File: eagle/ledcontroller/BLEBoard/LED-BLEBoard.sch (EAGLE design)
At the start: 18 parts, among them U1 FTSH-105-01-F-DV-ND, U2 RFD22301, U3 TPS61232, U4 V_REG_MIC2920, U5 7AAF-3

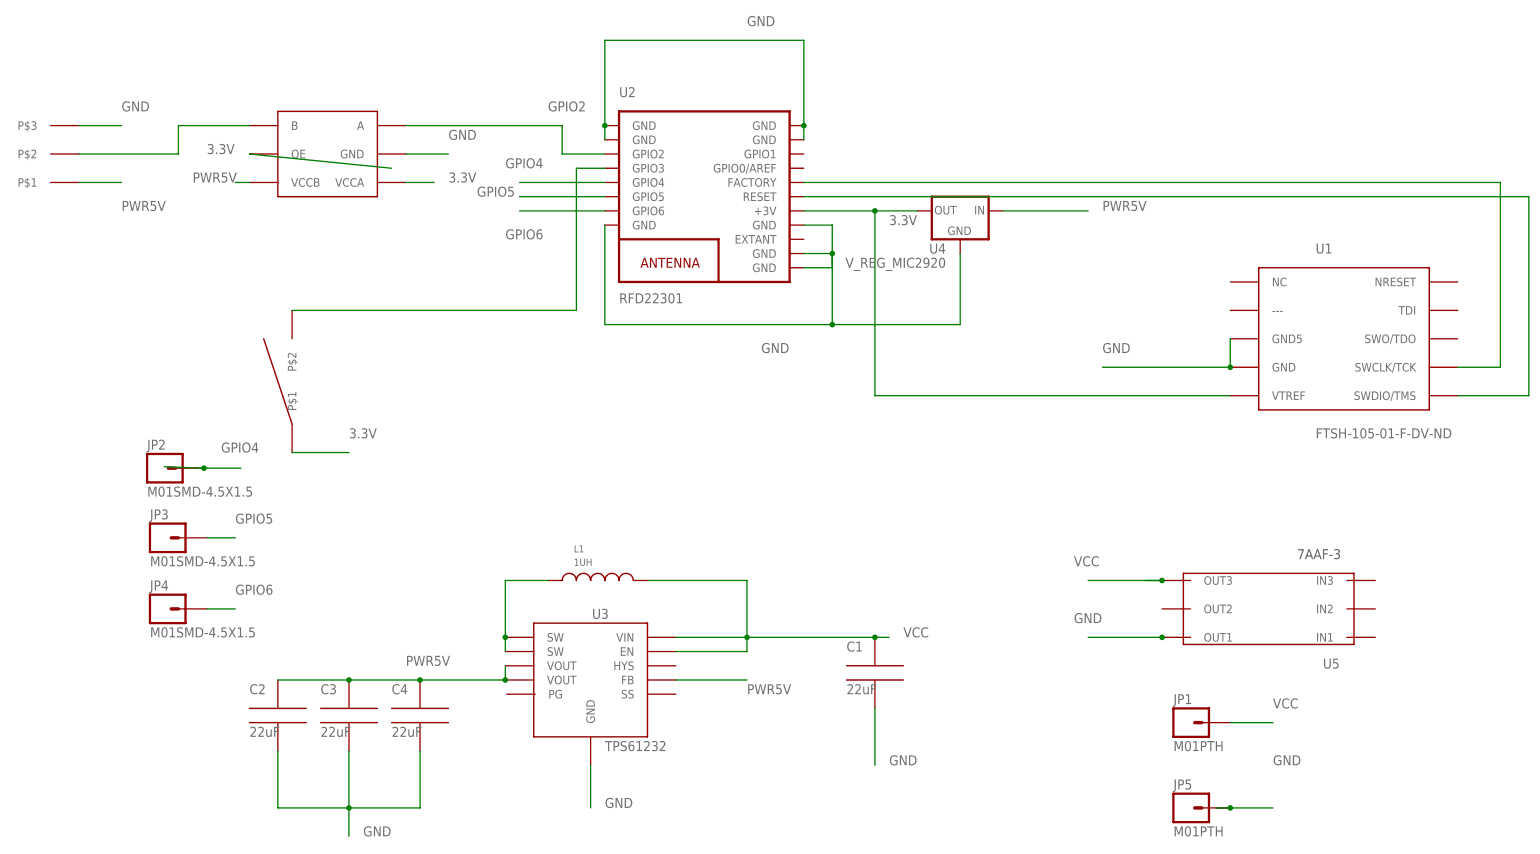
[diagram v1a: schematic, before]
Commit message: V0.8 added switch and re-layout
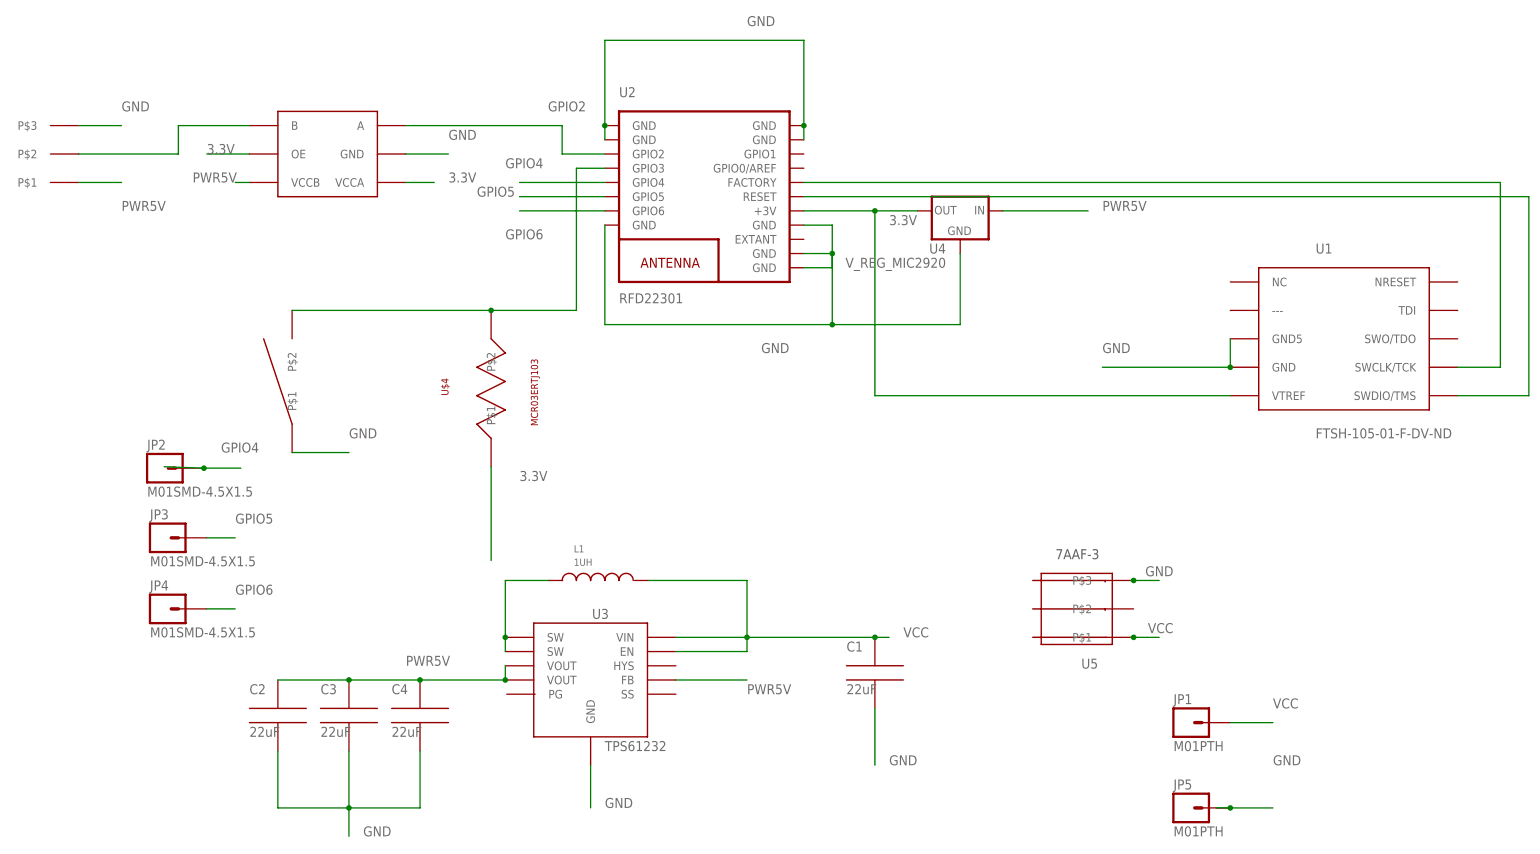
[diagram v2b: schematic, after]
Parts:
- added U$4: MCR03ERTJ103, bret:MCR03ERTJ103
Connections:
- net 3.3V: now also U$4.P$1; no longer U$3.P$1
- net GND: now also U$3.P$1, U5.P$3; no longer U5.OUT1
- net N$2: now also U$4.P$2
- net VCC: now also U5.P$1; no longer U5.OUT3
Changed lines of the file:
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@@
 <part name="JP1" library="SparkFun-Connectors" deviceset="M01" device="PTH"/>
 <part name="JP5" library="SparkFun-Connectors" deviceset="M01" device="PTH"/>
+<part name="U$4" library="bret" deviceset="MCR03ERTJ103" device=""/>
 </parts>
 <sheets>
@@
 <instance part="U1" gate="G$1" x="185.42" y="116.84"/>
 <instance part="U2" gate="G$1" x="48.26" y="139.7"/>
-<instance part="U5" gate="G$1" x="154.178" y="72.39" rot="R90"/>
+<instance part="U5" gate="G$1" x="110.998" y="72.39" rot="R90"/>
 <instance part="U$2" gate="G$1" x="-10.16" y="139.7" rot="R90"/>
 <instance part="U$1" gate="G$1" x="-63.5" y="142.24" rot="R90"/>
@@
 <instance part="JP1" gate="G$1" x="134.62" y="45.72"/>
 <instance part="JP5" gate="G$1" x="134.62" y="30.48"/>
+<instance part="U$4" gate="G$1" x="10.16" y="93.98" rot="R90"/>
 </instances>
 <busses>
@@
 </segment>
 <segment>
-<wire x1="127" y1="71.12" x2="130.048" y2="71.12" width="0.1524" layer="91"/>
-<label x="114.3" y="73.66" size="1.778" layer="95"/>
-<pinref part="U5" gate="G$1" pin="OUT3"/>
-<wire x1="130.048" y1="71.12" x2="116.84" y2="71.12" width="0.1524" layer="91"/>
-<junction x="130.048" y="71.12"/>
-</segment>
-<segment>
 <wire x1="142.24" y1="45.72" x2="149.86" y2="45.72" width="0.1524" layer="91"/>
 <label x="149.86" y="48.26" size="1.778" layer="95"/>
 <pinref part="JP1" gate="G$1" pin="1"/>
+</segment>
+<segment>
+<wire x1="129.54" y1="60.96" x2="124.968" y2="60.96" width="0.1524" layer="91"/>
+<pinref part="U5" gate="G$1" pin="P$1"/>
+<wire x1="124.968" y1="60.96" x2="124.46" y2="60.96" width="0.1524" layer="91"/>
+<junction x="124.968" y="60.96"/>
+<label x="132.08" y="63.5" size="1.778" layer="95" rot="R180"/>
 </segment>
 </net>
@@
 </segment>
 <segment>
-<wire x1="129.54" y1="60.96" x2="130.048" y2="60.96" width="0.1524" layer="91"/>
-<label x="114.3" y="63.5" size="1.778" layer="95"/>
-<pinref part="U5" gate="G$1" pin="OUT1"/>
-<wire x1="130.048" y1="60.96" x2="116.84" y2="60.96" width="0.1524" layer="91"/>
-<junction x="130.048" y="60.96"/>
-</segment>
-<segment>
 <wire x1="139.7" y1="30.48" x2="142.24" y2="30.48" width="0.1524" layer="91"/>
 <label x="149.86" y="38.1" size="1.778" layer="95"/>
@@
 <wire x1="-63.5" y1="152.4" x2="-55.88" y2="152.4" width="0.1524" layer="91"/>
 <label x="-55.88" y="154.94" size="1.778" layer="95"/>
+</segment>
+<segment>
+<pinref part="U$3" gate="G$1" pin="P$1"/>
+<wire x1="-25.4" y1="93.98" x2="-15.24" y2="93.98" width="0.1524" layer="91"/>
+<label x="-15.24" y="96.52" size="1.778" layer="95"/>
+</segment>
+<segment>
+<wire x1="129.54" y1="71.12" x2="124.968" y2="71.12" width="0.1524" layer="91"/>
+<pinref part="U5" gate="G$1" pin="P$3"/>
+<wire x1="124.968" y1="71.12" x2="124.46" y2="71.12" width="0.1524" layer="91"/>
+<junction x="124.968" y="71.12"/>
+<label x="132.08" y="73.66" size="1.778" layer="95" rot="R180"/>
 </segment>
 </net>
@@
 <segment>
 <pinref part="U$2" gate="G$1" pin="OE"/>
-<wire x1="-33.02" y1="147.32" x2="-7.62" y2="144.78" width="0.1524" layer="91"/>
+<wire x1="-33.02" y1="147.32" x2="-40.64" y2="147.32" width="0.1524" layer="91"/>
 <label x="-40.64" y="147.32" size="1.778" layer="95"/>
 </segment>
@@
 </segment>
 <segment>
-<pinref part="U$3" gate="G$1" pin="P$1"/>
-<wire x1="-25.4" y1="93.98" x2="-15.24" y2="93.98" width="0.1524" layer="91"/>
-<label x="-15.24" y="96.52" size="1.778" layer="95"/>
+<wire x1="10.16" y1="74.676" x2="10.16" y2="91.44" width="0.1524" layer="91"/>
+<label x="15.24" y="88.9" size="1.778" layer="95"/>
+<pinref part="U$4" gate="G$1" pin="P$1"/>
 </segment>
 </net>
@@
 <wire x1="25.4" y1="144.78" x2="25.4" y2="119.38" width="0.1524" layer="91"/>
 <pinref part="U$3" gate="G$1" pin="P$2"/>
-<wire x1="25.4" y1="119.38" x2="-25.4" y2="119.38" width="0.1524" layer="91"/>
+<wire x1="25.4" y1="119.38" x2="10.16" y2="119.38" width="0.1524" layer="91"/>
 <pinref part="U2" gate="G$1" pin="GPIO3"/>
+<wire x1="10.16" y1="119.38" x2="-25.4" y2="119.38" width="0.1524" layer="91"/>
 <wire x1="25.4" y1="144.78" x2="30.48" y2="144.78" width="0.1524" layer="91"/>
-</segment>
-</net>
+<pinref part="U$4" gate="G$1" pin="P$2"/>
+<junction x="10.16" y="119.38"/>
+</segment>
+</net>

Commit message: beginning
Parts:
- removed U4: V_REG_MIC2920, SparkFun-PowerIC:V_REG_MIC2920
- U5: value 7AAF-3 -> (none); device bret:7AAF-3 -> bret:TCR2EF33LM
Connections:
- net 3.3V: now also U5.VOUT; no longer U4.OUT
- net GND: now also U5.GND; no longer U4.GND, U5.P$3
- net PWR5V: now also U5.CTRL, U5.VIN; no longer U4.IN
- net VCC: no longer U5.P$1
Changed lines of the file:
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@@
 <setting verticaltext="up"/>
 </settings>
-<grid distance="0.1" unitdist="inch" unit="mm" style="lines" multiple="1" display="no" altdistance="0.01" altunitdist="inch" altunit="inch"/>
+<grid distance="0.1" unitdist="inch" unit="inch" style="lines" multiple="1" display="no" altdistance="0.01" altunitdist="inch" altunit="inch"/>
 <layers>
 <layer number="1" name="Top" color="4" fill="1" visible="no" active="no"/>
@@
 <part name="C1" library="bret" deviceset="C1.6X0.8MM" device="" value="22uF"/>
 <part name="U3" library="bret" deviceset="TPS61232" device="VSON" value="TPS61232"/>
-<part name="U4" library="SparkFun-PowerIC" deviceset="V_REG_MIC2920" device=""/>
 <part name="U1" library="bret" deviceset="FTSH-105-01-XXX-DV-K" device="" value="FTSH-105-01-F-DV-ND"/>
 <part name="U2" library="RF_Digital_RFD22301_Eagle_Schematic_PCB_Library" deviceset="RFD22301" device=""/>
-<part name="U5" library="bret" deviceset="7AAF-3" device="" value="7AAF-3"/>
 <part name="U$2" library="bret" deviceset="TXS0101" device="TXS0101DBVR" value="TXS0101TXS0101DBVR"/>
 <part name="U$1" library="bret" deviceset="MM800" device=""/>
@@
 <part name="JP5" library="SparkFun-Connectors" deviceset="M01" device="PTH"/>
 <part name="U$4" library="bret" deviceset="MCR03ERTJ103" device=""/>
+<part name="U5" library="bret" deviceset="TCR2EF33LM" device=""/>
 </parts>
 <sheets>
@@
 <instance part="C1" gate="G$1" x="81.28" y="45.72"/>
 <instance part="U3" gate="U1" x="27.94" y="53.34"/>
-<instance part="U4" gate="G$1" x="93.98" y="137.16" rot="MR0"/>
 <instance part="U1" gate="G$1" x="185.42" y="116.84"/>
 <instance part="U2" gate="G$1" x="48.26" y="139.7"/>
-<instance part="U5" gate="G$1" x="110.998" y="72.39" rot="R90"/>
 <instance part="U$2" gate="G$1" x="-10.16" y="139.7" rot="R90"/>
 <instance part="U$1" gate="G$1" x="-63.5" y="142.24" rot="R90"/>
@@
 <instance part="JP5" gate="G$1" x="134.62" y="30.48"/>
 <instance part="U$4" gate="G$1" x="10.16" y="93.98" rot="R90"/>
+<instance part="U5" gate="G$1" x="96.52" y="132.08"/>
 </instances>
 <busses>
@@
 <pinref part="JP1" gate="G$1" pin="1"/>
 </segment>
-<segment>
-<wire x1="129.54" y1="60.96" x2="124.968" y2="60.96" width="0.1524" layer="91"/>
-<pinref part="U5" gate="G$1" pin="P$1"/>
-<wire x1="124.968" y1="60.96" x2="124.46" y2="60.96" width="0.1524" layer="91"/>
-<junction x="124.968" y="60.96"/>
-<label x="132.08" y="63.5" size="1.778" layer="95" rot="R180"/>
-</segment>
 </net>
 <net name="GND" class="0">
@@
 <junction x="71.12" y="116.84"/>
 <label x="58.42" y="111.76" size="1.778" layer="95"/>
-<pinref part="U4" gate="G$1" pin="GND"/>
-<wire x1="93.98" y1="116.84" x2="93.98" y2="129.54" width="0.1524" layer="91"/>
+<wire x1="93.98" y1="116.84" x2="93.98" y2="127" width="0.1524" layer="91"/>
 <pinref part="U2" gate="G$1" pin="GND@3"/>
 <pinref part="U2" gate="G$1" pin="GND@4"/>
 <pinref part="U2" gate="G$1" pin="GND@5"/>
 <pinref part="U2" gate="G$1" pin="GND@6"/>
+<pinref part="U5" gate="G$1" pin="GND"/>
+<wire x1="93.98" y1="127" x2="96.52" y2="127" width="0.1524" layer="91"/>
 </segment>
 <segment>
@@
 <wire x1="-25.4" y1="93.98" x2="-15.24" y2="93.98" width="0.1524" layer="91"/>
 <label x="-15.24" y="96.52" size="1.778" layer="95"/>
-</segment>
-<segment>
-<wire x1="129.54" y1="71.12" x2="124.968" y2="71.12" width="0.1524" layer="91"/>
-<pinref part="U5" gate="G$1" pin="P$3"/>
-<wire x1="124.968" y1="71.12" x2="124.46" y2="71.12" width="0.1524" layer="91"/>
-<junction x="124.968" y="71.12"/>
-<label x="132.08" y="73.66" size="1.778" layer="95" rot="R180"/>
 </segment>
 </net>
@@
 </segment>
 <segment>
-<pinref part="U4" gate="G$1" pin="IN"/>
-<wire x1="101.6" y1="137.16" x2="116.84" y2="137.16" width="0.1524" layer="91"/>
-<label x="119.38" y="137.16" size="1.778" layer="95"/>
+<label x="93.98" y="134.62" size="1.778" layer="95"/>
+<pinref part="U5" gate="G$1" pin="VIN"/>
+<wire x1="96.52" y1="132.08" x2="91.44" y2="132.08" width="0.1524" layer="91"/>
 </segment>
 <segment>
@@
 <wire x1="-63.5" y1="142.24" x2="-55.88" y2="142.24" width="0.1524" layer="91"/>
 <label x="-55.88" y="137.16" size="1.778" layer="95"/>
+</segment>
+<segment>
+<pinref part="U5" gate="G$1" pin="CTRL"/>
+<wire x1="121.92" y1="132.08" x2="129.54" y2="132.08" width="0.1524" layer="91"/>
+<label x="116.84" y="134.62" size="1.778" layer="95"/>
 </segment>
 </net>
@@
 <net name="3.3V" class="0">
 <segment>
-<pinref part="U4" gate="G$1" pin="OUT"/>
-<wire x1="86.36" y1="137.16" x2="78.74" y2="137.16" width="0.1524" layer="91"/>
 <label x="81.28" y="134.62" size="1.778" layer="95"/>
 <wire x1="78.74" y1="137.16" x2="66.04" y2="137.16" width="0.1524" layer="91"/>
 <wire x1="142.24" y1="104.14" x2="78.74" y2="104.14" width="0.1524" layer="91"/>
-<wire x1="78.74" y1="104.14" x2="78.74" y2="137.16" width="0.1524" layer="91"/>
-<junction x="78.74" y="137.16"/>
+<wire x1="78.74" y1="104.14" x2="78.74" y2="121.92" width="0.1524" layer="91"/>
 <pinref part="U1" gate="G$1" pin="VTREF"/>
 <pinref part="U2" gate="G$1" pin="+3V"/>
-</segment>
-<segment>
+<pinref part="U5" gate="G$1" pin="VOUT"/>
+<wire x1="78.74" y1="121.92" x2="78.74" y2="137.16" width="0.1524" layer="91"/>
+<wire x1="78.74" y1="121.92" x2="96.52" y2="121.92" width="0.1524" layer="91"/>
+<junction x="78.74" y="121.92"/>
+</segment>
+<segment>
